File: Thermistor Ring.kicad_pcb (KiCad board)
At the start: 2 copper layers, 48.3 x 48.3 mm, 21 parts, among them J1 Conn_01x04_Socket, U1 TPS7A2018PDBVR, U2 MCP9808T-E/MC, U3 MCP9808T-E/MC, U4 MCP9808T-E/MC, U5 MCP9808T-E/MC, U6 MCP9808T-E/MC, U7 MCP9808T-E/MC

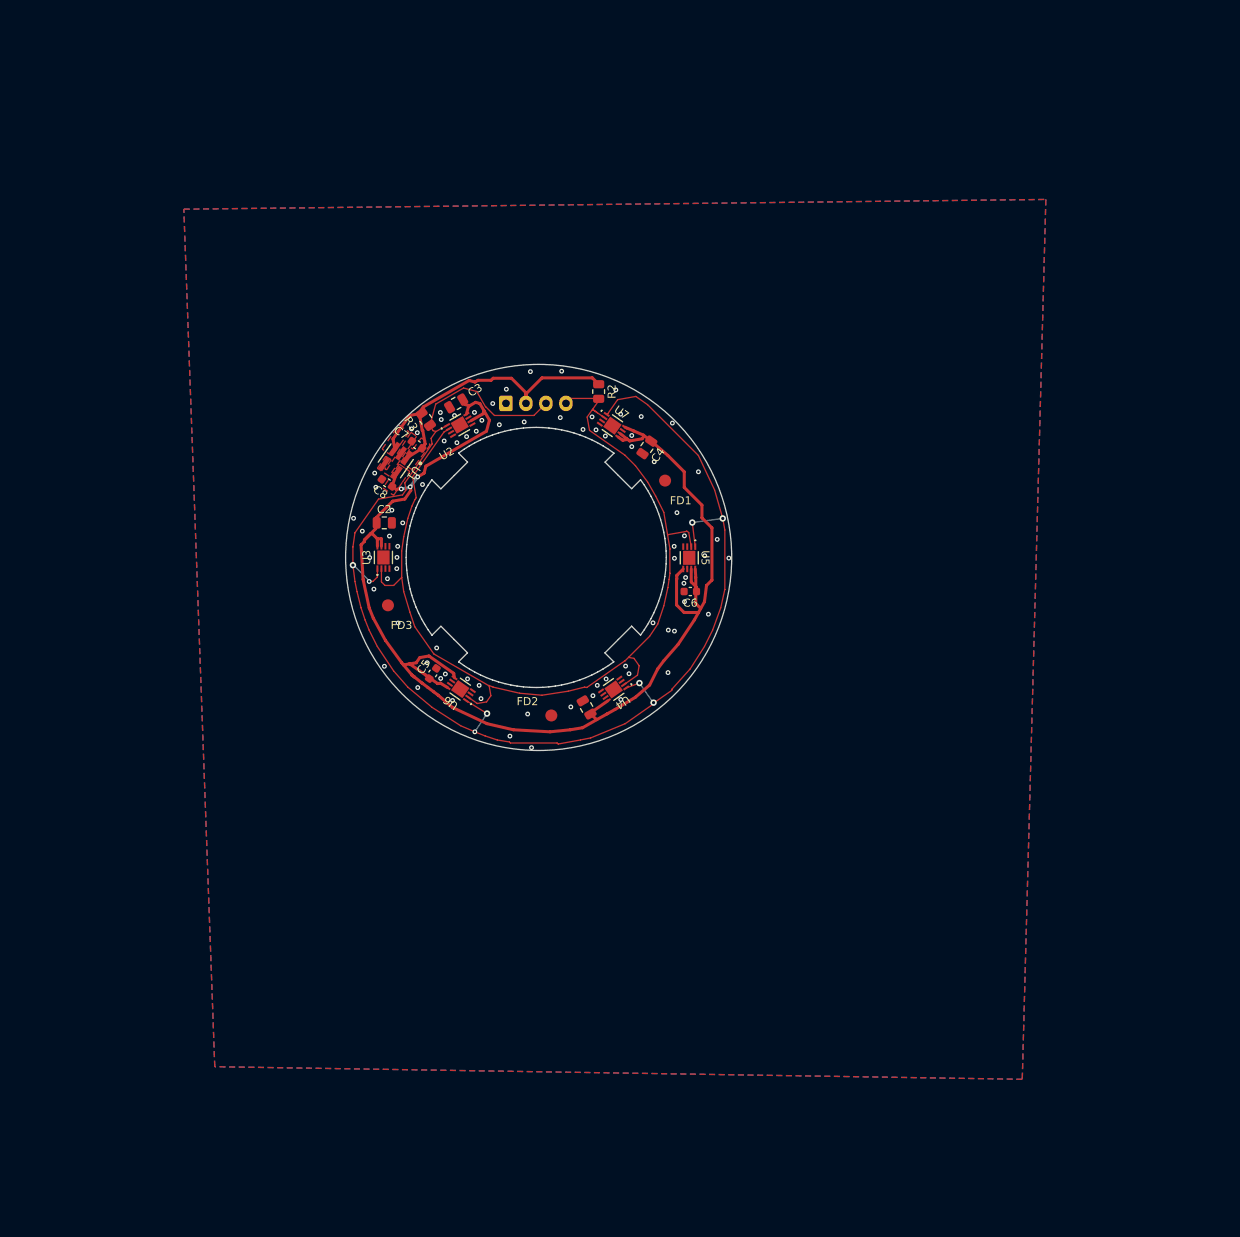
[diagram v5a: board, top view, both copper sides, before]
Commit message: Reduce size of epad, improve layout
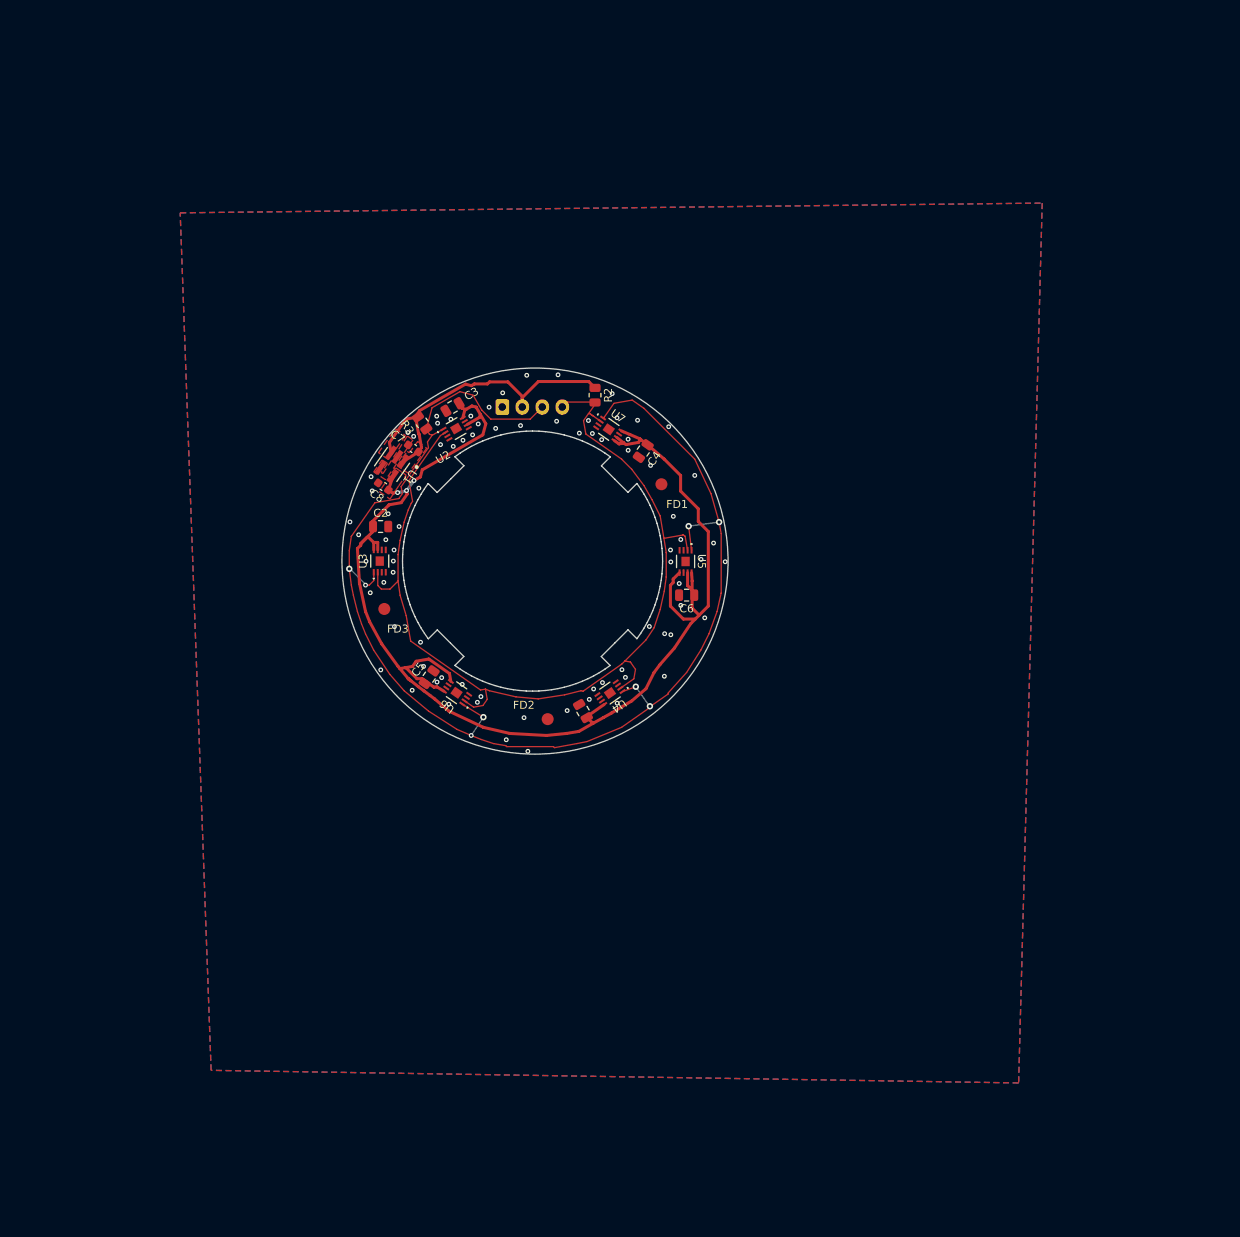
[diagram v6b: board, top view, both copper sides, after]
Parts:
- C5, C6: footprint Capacitor_SMD:C_0603_1608Metric -> Capacitor_SMD:C_0805_2012Metric
- moved C4 0.64 mm to (89.1, 42.2)
- moved U5 0.64 mm to (94.4, 56.0)
- moved C7 0.64 mm to (60.4, 41.9)
- moved R3 0.64 mm to (61.5, 38.7)
- moved U3 0.64 mm to (56.2, 55.9)
- moved U1 0.64 mm to (57.7, 43.9)
- moved U7 0.64 mm to (84.8, 39.5)
- moved FD3 0.64 mm to (56.7, 61.9)
- moved C2 0.64 mm to (56.3, 51.6)
- moved U2 0.64 mm to (65.7, 39.4)
- moved R2 0.64 mm to (83.1, 35.2)
- moved C6 0.64 mm to (94.5, 60.2)
- moved C8 0.64 mm to (56.6, 46.6)
- moved FD1 0.64 mm to (91.4, 46.3)
- moved J1 0.64 mm to (71.5, 36.7)
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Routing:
- net /VDD: track 170.8 -> 172.5 mm
- net GND: vias 80 -> 79

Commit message: Change to MSOP thermistor
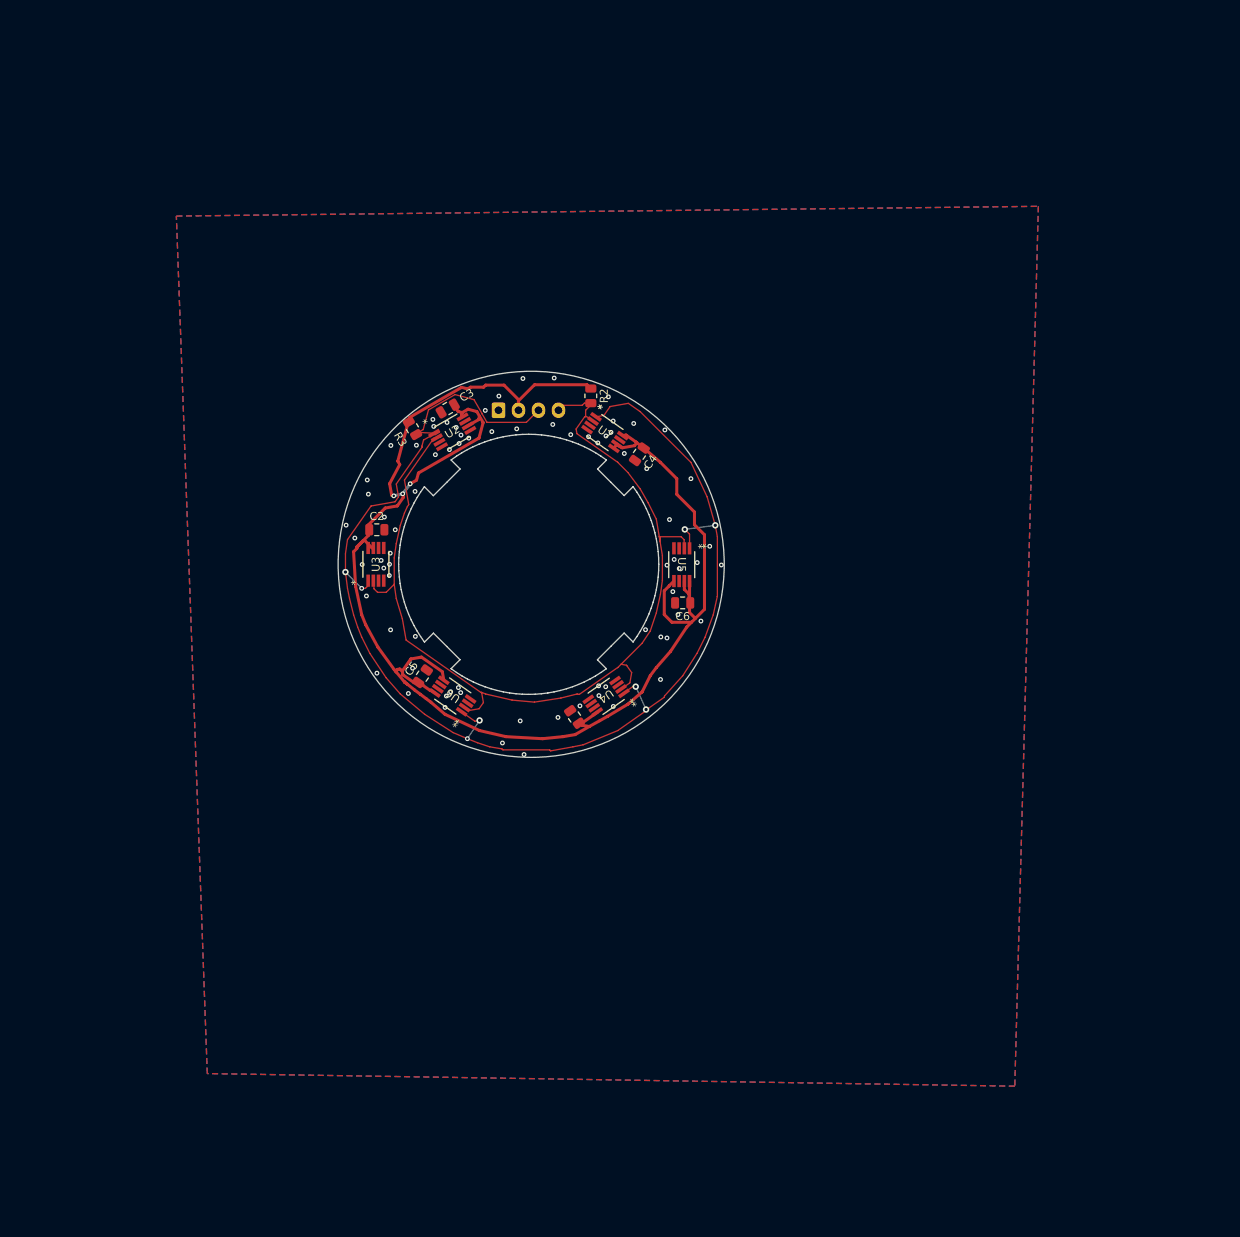
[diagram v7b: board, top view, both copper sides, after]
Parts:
- removed C7, C8: 1.0uF, Capacitor_SMD:C_0603_1608Metric
- removed FD1, FD2, FD3: Fiducial_1.5mm_Mask3mm, Fiducial:Fiducial_1.5mm_Mask3mm
- removed U1: TPS7A2018PDBVR, TPS7A2018PDBVR:DBV0005A-IPC_A
- U2, U3, U4, U5, U6, U7: footprint MCP9808T-E:DFN8_2x3MC_MCH -> MCP9808-E/MS:MSOP8_MC_MCH
- moved R3 1.38 mm to (60.2, 39.3), turned to -60 degrees
- moved C1 1.29 mm to (80.5, 75.4), turned to 125 degrees
- moved C6 1.09 mm to (94.0, 61.2)
- moved C5 0.85 mm to (61.5, 70.3)
- moved U2 0.63 mm to (65.2, 39.8)
- moved U6 0.63 mm to (65.3, 72.8)
- moved U3 0.63 mm to (55.7, 56.3)
- moved J1 0.63 mm to (71.0, 37.1)
- moved C2 0.63 mm to (55.8, 52.0)
- moved U7 0.63 mm to (84.3, 39.9)
- moved U5 0.63 mm to (93.9, 56.4)
- moved C4 0.63 mm to (88.6, 42.6)
- moved U4 0.63 mm to (84.5, 72.8)
- moved C3 0.62 mm to (64.7, 36.9)
- moved R2 0.53 mm to (82.5, 35.3)
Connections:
- C1 pad 1: /VDD -> /Power 3.3-5V
- C2 pad 1: /VDD -> /Power 3.3-5V
- C3 pad 1: /VDD -> /Power 3.3-5V
- C4 pad 1: /VDD -> /Power 3.3-5V
- C5 pad 1: /VDD -> /Power 3.3-5V
- C6 pad 1: /VDD -> /Power 3.3-5V
- U2 pad 3: GND -> unconnected-(U2-ALERT-Pad3)
- U2 pad 6: /VDD -> /Power 3.3-5V
- U2 pad 8: /VDD -> /Power 3.3-5V
- U3 pad 3: GND -> unconnected-(U3-ALERT-Pad3)
- U3 pad 7: /VDD -> /Power 3.3-5V
- U3 pad 8: /VDD -> /Power 3.3-5V
- U4 pad 3: GND -> unconnected-(U4-ALERT-Pad3)
- U4 pad 8: /VDD -> /Power 3.3-5V
- U5 pad 3: GND -> unconnected-(U5-ALERT-Pad3)
- U5 pad 5: /VDD -> /Power 3.3-5V
- U5 pad 7: /VDD -> /Power 3.3-5V
- U5 pad 8: /VDD -> /Power 3.3-5V
- U6 pad 3: GND -> unconnected-(U6-ALERT-Pad3)
- U6 pad 5: /VDD -> /Power 3.3-5V
- U6 pad 8: /VDD -> /Power 3.3-5V
- U7 pad 3: GND -> unconnected-(U7-ALERT-Pad3)
- U7 pad 5: /VDD -> /Power 3.3-5V
- U7 pad 6: /VDD -> /Power 3.3-5V
- U7 pad 8: /VDD -> /Power 3.3-5V
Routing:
- net /VDD: track 172.5 -> 0.00 mm, vias 3 -> 0
- net /Power 3.3-5V: track 41.6 -> 204.1 mm, vias 0 -> 3
- net /SDA: track 167.4 -> 169.3 mm
- net GND: track 0.33 -> 0.00 mm, vias 79 -> 77
- removed copper zone on F.Cu, net /Power 3.3-5V
- removed copper zone on F.Cu, net /VDD
